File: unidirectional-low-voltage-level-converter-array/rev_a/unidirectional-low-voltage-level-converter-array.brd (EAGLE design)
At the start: 20.3 x 34.3 mm, 12 parts

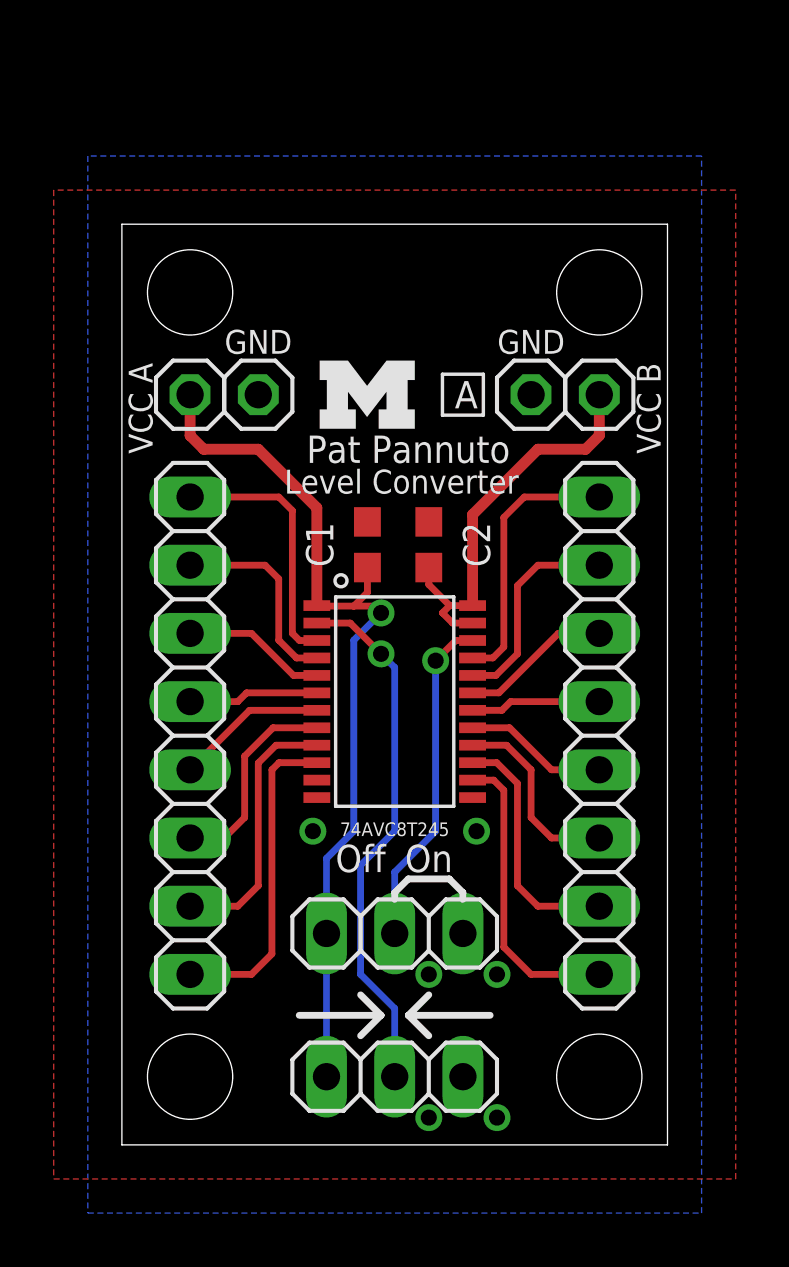
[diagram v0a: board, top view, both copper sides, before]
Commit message: Restrict stop layers to board dim, clean up silkscreen
The stop layer isn't clipped by the CAM job, so do it by hand.
Make Brad a little happier on the silkscreen. Whatever Brad, it was fine.
Put the bottom left corner on the origin.
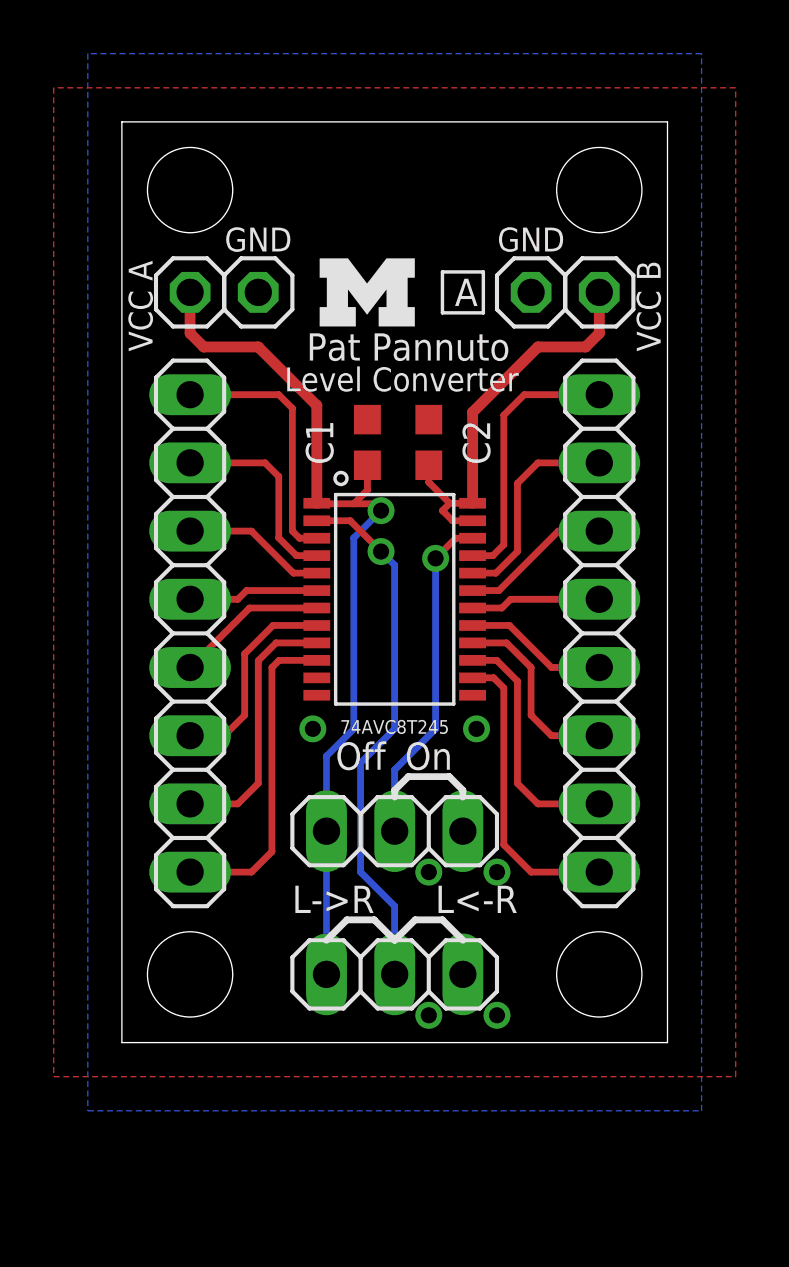
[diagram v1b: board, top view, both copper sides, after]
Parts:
- moved JP1 3.81 mm to (2.54, 27.9)
- moved JP2 3.81 mm to (17.8, 27.9)
- moved JP3 3.81 mm to (5.08, 27.9)
- moved JP4 3.81 mm to (15.2, 27.9)
- moved LOGO1 3.81 mm to (7.37, 26.7)
- moved U$1 3.81 mm to (10.2, 16.5)
- moved A 3.81 mm to (2.54, 15.2)
- moved B 3.81 mm to (17.8, 15.2)
- moved DIR 3.81 mm to (10.2, 2.54)
- moved !OE 3.81 mm to (10.2, 7.87)
- moved C1 3.81 mm to (9.14, 22.4)
- moved C2 3.81 mm to (11.4, 22.4)
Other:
- board text added: "L->R"
- board text added: "L<-R"
